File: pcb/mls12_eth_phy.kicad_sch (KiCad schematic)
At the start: 21 parts, among them U1 KSZ8081RNA, Y1 25MHz

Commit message: Update to 25W PoE+ module, 2 outputs
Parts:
- renumbered C13 to C11, C14 to C12, C15 to C13, C16 to C14, C17 to C15, C18 to C16, C19 to C17, C20 to C18, D5 to D6, FB13 to FB7, U1 to U2
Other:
- company: (none) -> Quomodo BV
- title: Ethernet & PoE -> Ethernet PHY
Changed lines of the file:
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@@
 	(paper "A4")
 	(title_block
-		(title "Ethernet & PoE")
-		(date "2025-07-25")
+		(title "Ethernet PHY")
+		(date "2025-07-26")
 		(rev "A")
+		(company "Quomodo BV")
 	)
 	(text "Ethernet routing checklist"
@@
 		(dnp no)
 		(fields_autoplaced yes)
-		(property "Reference" "#PWR017"
+		(property "Reference" "#PWR019"
 			(at 144.78 59.69 0)
 			(effects
@@
 			(project "mls12"
 				(path "/53bda2f8-fdf0-44f4-aced-3b46017d299c/f9d4ebc4-b22e-4ea3-9755-37111373d6cf"
-					(reference "#PWR017")
+					(reference "#PWR019")
 					(unit 1)
 				)
@@
 		(on_board yes)
 		(dnp no)
-		(property "Reference" "FB13"
+		(property "Reference" "FB7"
 			(at 132.08 39.624 90)
 			(effects
@@
 			(project "mls12"
 				(path "/53bda2f8-fdf0-44f4-aced-3b46017d299c/f9d4ebc4-b22e-4ea3-9755-37111373d6cf"
-					(reference "FB13")
+					(reference "FB7")
 					(unit 1)
 				)
@@
 		(dnp no)
 		(fields_autoplaced yes)
-		(property "Reference" "#PWR014"
+		(property "Reference" "#PWR016"
 			(at 127 41.91 0)
 			(effects
@@
 			(project "mls12"
 				(path "/53bda2f8-fdf0-44f4-aced-3b46017d299c/f9d4ebc4-b22e-4ea3-9755-37111373d6cf"
-					(reference "#PWR014")
+					(reference "#PWR016")
 					(unit 1)
 				)
@@
 		(dnp no)
 		(fields_autoplaced yes)
-		(property "Reference" "#PWR020"
+		(property "Reference" "#PWR022"
 			(at 157.48 77.47 0)
 			(effects
@@
 			(project "mls12"
 				(path "/53bda2f8-fdf0-44f4-aced-3b46017d299c/f9d4ebc4-b22e-4ea3-9755-37111373d6cf"
-					(reference "#PWR020")
+					(reference "#PWR022")
 					(unit 1)
 				)
@@
 		(dnp yes)
 		(fields_autoplaced yes)
-		(property "Reference" "C20"
+		(property "Reference" "C18"
 			(at 173.99 140.9699 0)
 			(effects
@@
 			(project "mls12"
 				(path "/53bda2f8-fdf0-44f4-aced-3b46017d299c/f9d4ebc4-b22e-4ea3-9755-37111373d6cf"
-					(reference "C20")
+					(reference "C18")
 					(unit 1)
 				)
@@
 		(dnp no)
 		(fields_autoplaced yes)
-		(property "Reference" "#PWR013"
+		(property "Reference" "#PWR015"
 			(at 114.3 138.43 0)
 			(effects
@@
 			(project "mls12"
 				(path "/53bda2f8-fdf0-44f4-aced-3b46017d299c/f9d4ebc4-b22e-4ea3-9755-37111373d6cf"
-					(reference "#PWR013")
+					(reference "#PWR015")
 					(unit 1)
 				)
@@
 		(dnp no)
 		(fields_autoplaced yes)
-		(property "Reference" "#PWR023"
+		(property "Reference" "#PWR025"
 			(at 213.36 107.95 0)
 			(effects
@@
 			(project "mls12"
 				(path "/53bda2f8-fdf0-44f4-aced-3b46017d299c/f9d4ebc4-b22e-4ea3-9755-37111373d6cf"
-					(reference "#PWR023")
+					(reference "#PWR025")
 					(unit 1)
 				)
@@
 		(dnp no)
 		(fields_autoplaced yes)
-		(property "Reference" "#PWR016"
+		(property "Reference" "#PWR018"
 			(at 135.89 138.43 0)
 			(effects
@@
 			(project "mls12"
 				(path "/53bda2f8-fdf0-44f4-aced-3b46017d299c/f9d4ebc4-b22e-4ea3-9755-37111373d6cf"
-					(reference "#PWR016")
+					(reference "#PWR018")
 					(unit 1)
 				)
@@
 		(dnp no)
 		(fields_autoplaced yes)
-		(property "Reference" "#PWR018"
+		(property "Reference" "#PWR020"
 			(at 144.78 77.47 0)
 			(effects
@@
 			(project "mls12"
 				(path "/53bda2f8-fdf0-44f4-aced-3b46017d299c/f9d4ebc4-b22e-4ea3-9755-37111373d6cf"
-					(reference "#PWR018")
+					(reference "#PWR020")
 					(unit 1)
 				)
@@
 		(dnp no)
 		(fields_autoplaced yes)
-		(property "Reference" "C18"
+		(property "Reference" "C16"
 			(at 161.29 64.7699 0)
 			(effects
@@
 			(project "mls12"
 				(path "/53bda2f8-fdf0-44f4-aced-3b46017d299c/f9d4ebc4-b22e-4ea3-9755-37111373d6cf"
-					(reference "C18")
+					(reference "C16")
 					(unit 1)
 				)
@@
 		(on_board yes)
 		(dnp no)
-		(property "Reference" "U1"
+		(property "Reference" "U2"
 			(at 133.7467 129.54 0)
 			(effects
@@
 			(project "mls12"
 				(path "/53bda2f8-fdf0-44f4-aced-3b46017d299c/f9d4ebc4-b22e-4ea3-9755-37111373d6cf"
-					(reference "U1")
+					(reference "U2")
 					(unit 1)
 				)
@@
 		(on_board yes)
 		(dnp no)
-		(property "Reference" "C13"
+		(property "Reference" "C11"
 			(at 110.49 64.7699 0)
 			(effects
@@
 			(project "mls12"
 				(path "/53bda2f8-fdf0-44f4-aced-3b46017d299c/f9d4ebc4-b22e-4ea3-9755-37111373d6cf"
-					(reference "C13")
+					(reference "C11")
 					(unit 1)
 				)
@@
 		(on_board yes)
 		(dnp no)
-		(property "Reference" "D5"
+		(property "Reference" "D6"
 			(at 241.3 110.4899 90)
 			(effects
@@
 			(project ""
 				(path "/53bda2f8-fdf0-44f4-aced-3b46017d299c/f9d4ebc4-b22e-4ea3-9755-37111373d6cf"
-					(reference "D5")
+					(reference "D6")
 					(unit 1)
 				)
@@
 		(on_board yes)
 		(dnp no)
-		(property "Reference" "C15"
+		(property "Reference" "C13"
 			(at 148.082 46.99 0)
 			(effects
@@
 			(project "mls12"
 				(path "/53bda2f8-fdf0-44f4-aced-3b46017d299c/f9d4ebc4-b22e-4ea3-9755-37111373d6cf"
-					(reference "C15")
+					(reference "C13")
 					(unit 1)
 				)
@@
 		(dnp no)
 		(fields_autoplaced yes)
-		(property "Reference" "#PWR024"
+		(property "Reference" "#PWR026"
 			(at 236.22 109.22 0)
 			(effects
@@
 			(project "mls12"
 				(path "/53bda2f8-fdf0-44f4-aced-3b46017d299c/f9d4ebc4-b22e-4ea3-9755-37111373d6cf"
-					(reference "#PWR024")
+					(reference "#PWR026")
 					(unit 1)
 				)
@@
 		(dnp no)
 		(fields_autoplaced yes)
-		(property "Reference" "#PWR019"
+		(property "Reference" "#PWR021"
 			(at 157.48 59.69 0)
 			(effects
@@
 			(project "mls12"
 				(path "/53bda2f8-fdf0-44f4-aced-3b46017d299c/f9d4ebc4-b22e-4ea3-9755-37111373d6cf"
-					(reference "#PWR019")
+					(reference "#PWR021")
 					(unit 1)
 				)
@@
 		(dnp yes)
 		(fields_autoplaced yes)
-		(property "Reference" "C19"
+		(property "Reference" "C17"
 			(at 173.99 125.7299 0)
 			(effects
@@
 			(project "mls12"
 				(path "/53bda2f8-fdf0-44f4-aced-3b46017d299c/f9d4ebc4-b22e-4ea3-9755-37111373d6cf"
-					(reference "C19")
+					(reference "C17")
 					(unit 1)
 				)
@@
 		(dnp no)
 		(fields_autoplaced yes)
-		(property "Reference" "C17"
+		(property "Reference" "C15"
 			(at 161.29 46.9899 0)
 			(effects
@@
 			(project "mls12"
 				(path "/53bda2f8-fdf0-44f4-aced-3b46017d299c/f9d4ebc4-b22e-4ea3-9755-37111373d6cf"
-					(reference "C17")
+					(reference "C15")
 					(unit 1)
 				)
@@
 		(dnp no)
 		(fields_autoplaced yes)
-		(property "Reference" "#PWR015"
+		(property "Reference" "#PWR017"
 			(at 127 77.47 0)
 			(effects
@@
 			(project "mls12"
 				(path "/53bda2f8-fdf0-44f4-aced-3b46017d299c/f9d4ebc4-b22e-4ea3-9755-37111373d6cf"
-					(reference "#PWR015")
+					(reference "#PWR017")
 					(unit 1)
 				)
@@
 		(dnp no)
 		(fields_autoplaced yes)
-		(property "Reference" "#PWR012"
+		(property "Reference" "#PWR014"
 			(at 114.3 77.47 0)
 			(effects
@@
 			(project "mls12"
 				(path "/53bda2f8-fdf0-44f4-aced-3b46017d299c/f9d4ebc4-b22e-4ea3-9755-37111373d6cf"
-					(reference "#PWR012")
+					(reference "#PWR014")
 					(unit 1)
 				)
@@
 		(on_board yes)
 		(dnp no)
-		(property "Reference" "C16"
+		(property "Reference" "C14"
 			(at 148.082 64.77 0)
 			(effects
@@
 			(project "mls12"
 				(path "/53bda2f8-fdf0-44f4-aced-3b46017d299c/f9d4ebc4-b22e-4ea3-9755-37111373d6cf"
-					(reference "C16")
+					(reference "C14")
 					(unit 1)
 				)
@@
 		(dnp no)
 		(fields_autoplaced yes)
-		(property "Reference" "#PWR021"
+		(property "Reference" "#PWR023"
 			(at 166.37 142.24 0)
 			(effects
@@
 			(project "mls12"
 				(path "/53bda2f8-fdf0-44f4-aced-3b46017d299c/f9d4ebc4-b22e-4ea3-9755-37111373d6cf"
-					(reference "#PWR021")
+					(reference "#PWR023")
 					(unit 1)
 				)
@@
 		(dnp no)
 		(fields_autoplaced yes)
-		(property "Reference" "#PWR022"
+		(property "Reference" "#PWR024"
 			(at 194.31 142.24 0)
 			(effects
@@
 			(project "mls12"
 				(path "/53bda2f8-fdf0-44f4-aced-3b46017d299c/f9d4ebc4-b22e-4ea3-9755-37111373d6cf"
-					(reference "#PWR022")
+					(reference "#PWR024")
 					(unit 1)
 				)
@@
 		(on_board yes)
 		(dnp no)
-		(property "Reference" "C14"
+		(property "Reference" "C12"
 			(at 123.698 64.77 0)
 			(effects
@@
 			(project "mls12"
 				(path "/53bda2f8-fdf0-44f4-aced-3b46017d299c/f9d4ebc4-b22e-4ea3-9755-37111373d6cf"
-					(reference "C14")
+					(reference "C12")
 					(unit 1)
 				)

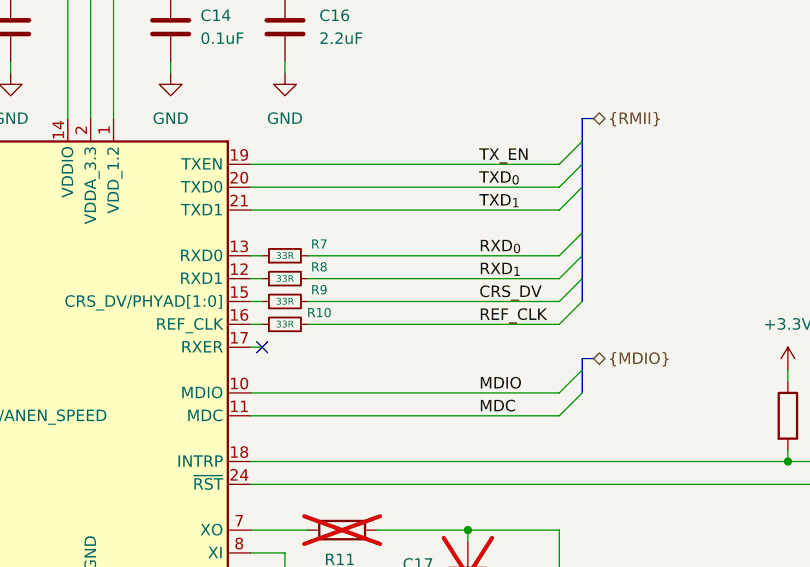
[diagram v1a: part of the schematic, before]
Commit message: Initial RMII, MDIO routing
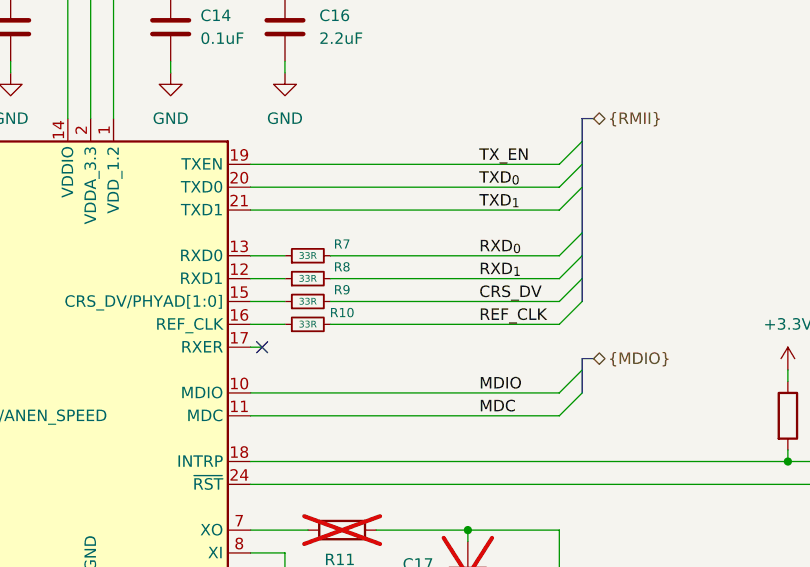
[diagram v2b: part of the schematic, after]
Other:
- moved on the sheet: R10, R7, R8, R9
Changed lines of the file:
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@@
 	(wire
 		(pts
-			(xy 160.02 99.06) (xy 187.96 99.06)
+			(xy 162.56 99.06) (xy 187.96 99.06)
 		)
 		(stroke
@@
 	(wire
 		(pts
-			(xy 160.02 91.44) (xy 187.96 91.44)
+			(xy 162.56 91.44) (xy 187.96 91.44)
 		)
 		(stroke
@@
 	(wire
 		(pts
-			(xy 153.67 93.98) (xy 154.94 93.98)
+			(xy 153.67 93.98) (xy 157.48 93.98)
 		)
 		(stroke
@@
 	(wire
 		(pts
-			(xy 153.67 99.06) (xy 154.94 99.06)
+			(xy 153.67 99.06) (xy 157.48 99.06)
 		)
 		(stroke
@@
 	(wire
 		(pts
-			(xy 160.02 96.52) (xy 187.96 96.52)
+			(xy 162.56 96.52) (xy 187.96 96.52)
 		)
 		(stroke
@@
 	(wire
 		(pts
-			(xy 160.02 93.98) (xy 187.96 93.98)
+			(xy 162.56 93.98) (xy 187.96 93.98)
 		)
 		(stroke
@@
 	(wire
 		(pts
-			(xy 153.67 96.52) (xy 154.94 96.52)
+			(xy 153.67 96.52) (xy 157.48 96.52)
 		)
 		(stroke
@@
 	(wire
 		(pts
-			(xy 153.67 91.44) (xy 154.94 91.44)
+			(xy 153.67 91.44) (xy 157.48 91.44)
 		)
 		(stroke
@@
 		(polyline
 			(pts
-				(xy 167.64 100.33) (xy 170.18 100.33) (xy 170.18 80.01) (xy 167.64 80.01)
+				(xy 156.21 100.33) (xy 175.26 100.33) (xy 175.26 80.01) (xy 156.21 80.01)
 			)
 			(stroke
@@
 		(length 2.54)
 		(shape round)
-		(at 168.91 80.01 0)
+		(at 163.83 80.01 0)
 		(fields_autoplaced yes)
 		(effects
@@
 		)
 		(property "Netclass" "RMII_50R"
-			(at 169.6085 77.47 0)
+			(at 164.5285 77.47 0)
 			(effects
 				(font
@@
 		)
 		(property "Component Class" ""
-			(at 408.94 8.89 0)
+			(at 403.86 8.89 0)
 			(effects
 				(font
@@
 	(symbol
 		(lib_id "Device:R_Small")
-		(at 157.48 93.98 90)
+		(at 160.02 93.98 90)
 		(unit 1)
 		(exclude_from_sim no)
@@
 		(dnp no)
 		(property "Reference" "R8"
-			(at 161.29 92.71 90)
+			(at 163.83 92.71 90)
 			(effects
 				(font
@@
 		)
 		(property "Value" "33R"
-			(at 157.48 93.98 90)
+			(at 160.02 93.98 90)
 			(effects
 				(font
@@
 		)
 		(property "Footprint" "Resistor_SMD:R_0603_1608Metric"
-			(at 157.48 93.98 0)
+			(at 160.02 93.98 0)
 			(effects
 				(font
@@
 		)
 		(property "Datasheet" "https://www.mouser.be/datasheet/2/210/ASC_WR-3314721.pdf"
-			(at 157.48 93.98 0)
+			(at 160.02 93.98 0)
 			(effects
 				(font
@@
 		)
 		(property "Description" "Resistor, small symbol"
-			(at 157.48 93.98 0)
+			(at 160.02 93.98 0)
 			(effects
 				(font
@@
 		)
 		(property "MF" "Walsin"
-			(at 157.48 93.98 90)
+			(at 160.02 93.98 90)
 			(effects
 				(font
@@
 		)
 		(property "MPN" "WR06X330 JTL"
-			(at 157.48 93.98 90)
+			(at 160.02 93.98 90)
 			(effects
 				(font
@@
 		)
 		(property "TODO" ""
-			(at 157.48 93.98 90)
+			(at 160.02 93.98 90)
 			(effects
 				(font
@@
 	(symbol
 		(lib_id "Device:R_Small")
-		(at 157.48 99.06 90)
+		(at 160.02 99.06 90)
 		(unit 1)
 		(exclude_from_sim no)
@@
 		(dnp no)
 		(property "Reference" "R10"
-			(at 161.29 97.79 90)
+			(at 163.83 97.79 90)
 			(effects
 				(font
@@
 		)
 		(property "Value" "33R"
-			(at 157.48 99.06 90)
+			(at 160.02 99.06 90)
 			(effects
 				(font
@@
 		)
 		(property "Footprint" "Resistor_SMD:R_0603_1608Metric"
-			(at 157.48 99.06 0)
+			(at 160.02 99.06 0)
 			(effects
 				(font
@@
 		)
 		(property "Datasheet" "https://www.mouser.be/datasheet/2/210/ASC_WR-3314721.pdf"
-			(at 157.48 99.06 0)
+			(at 160.02 99.06 0)
 			(effects
 				(font
@@
 		)
 		(property "Description" "Resistor, small symbol"
-			(at 157.48 99.06 0)
+			(at 160.02 99.06 0)
 			(effects
 				(font
@@
 		)
 		(property "MF" "Walsin"
-			(at 157.48 99.06 90)
+			(at 160.02 99.06 90)
 			(effects
 				(font
@@
 		)
 		(property "MPN" "WR06X330 JTL"
-			(at 157.48 99.06 90)
+			(at 160.02 99.06 90)
 			(effects
 				(font
@@
 		)
 		(property "TODO" ""
-			(at 157.48 99.06 90)
+			(at 160.02 99.06 90)
 			(effects
 				(font
@@
 	(symbol
 		(lib_id "Device:R_Small")
-		(at 157.48 96.52 90)
+		(at 160.02 96.52 90)
 		(unit 1)
 		(exclude_from_sim no)
@@
 		(dnp no)
 		(property "Reference" "R9"
-			(at 161.29 95.25 90)
+			(at 163.83 95.25 90)
 			(effects
 				(font
@@
 		)
 		(property "Value" "33R"
-			(at 157.48 96.52 90)
+			(at 160.02 96.52 90)
 			(effects
 				(font
@@
 		)
 		(property "Footprint" "Resistor_SMD:R_0603_1608Metric"
-			(at 157.48 96.52 0)
+			(at 160.02 96.52 0)
 			(effects
 				(font
@@
 		)
 		(property "Datasheet" "https://www.mouser.be/datasheet/2/210/ASC_WR-3314721.pdf"
-			(at 157.48 96.52 0)
+			(at 160.02 96.52 0)
 			(effects
 				(font
@@
 		)
 		(property "Description" "Resistor, small symbol"
-			(at 157.48 96.52 0)
+			(at 160.02 96.52 0)
 			(effects
 				(font
@@
 		)
 		(property "MF" "Walsin"
-			(at 157.48 96.52 90)
+			(at 160.02 96.52 90)
 			(effects
 				(font
@@
 		)
 		(property "MPN" "WR06X330 JTL"
-			(at 157.48 96.52 90)
+			(at 160.02 96.52 90)
 			(effects
 				(font
@@
 		)
 		(property "TODO" ""
-			(at 157.48 96.52 90)
+			(at 160.02 96.52 90)
 			(effects
 				(font
@@
 	(symbol
 		(lib_id "Device:R_Small")
-		(at 157.48 91.44 90)
+		(at 160.02 91.44 90)
 		(unit 1)
 		(exclude_from_sim no)
@@
 		(dnp no)
 		(property "Reference" "R7"
-			(at 161.29 90.17 90)
+			(at 163.83 90.17 90)
 			(effects
 				(font
@@
 		)
 		(property "Value" "33R"
-			(at 157.48 91.44 90)
+			(at 160.02 91.44 90)
 			(effects
 				(font
@@
 		)
 		(property "Footprint" "Resistor_SMD:R_0603_1608Metric"
-			(at 157.48 91.44 0)
+			(at 160.02 91.44 0)
 			(effects
 				(font
@@
 		)
 		(property "Datasheet" "https://www.mouser.be/datasheet/2/210/ASC_WR-3314721.pdf"
-			(at 157.48 91.44 0)
+			(at 160.02 91.44 0)
 			(effects
 				(font
@@
 		)
 		(property "Description" "Resistor, small symbol"
-			(at 157.48 91.44 0)
+			(at 160.02 91.44 0)
 			(effects
 				(font
@@
 		)
 		(property "MF" "Walsin"
-			(at 157.48 91.44 90)
+			(at 160.02 91.44 90)
 			(effects
 				(font
@@
 		)
 		(property "MPN" "WR06X330 JTL"
-			(at 157.48 91.44 90)
+			(at 160.02 91.44 90)
 			(effects
 				(font
@@
 		)
 		(property "TODO" ""
-			(at 157.48 91.44 90)
+			(at 160.02 91.44 90)
 			(effects
 				(font

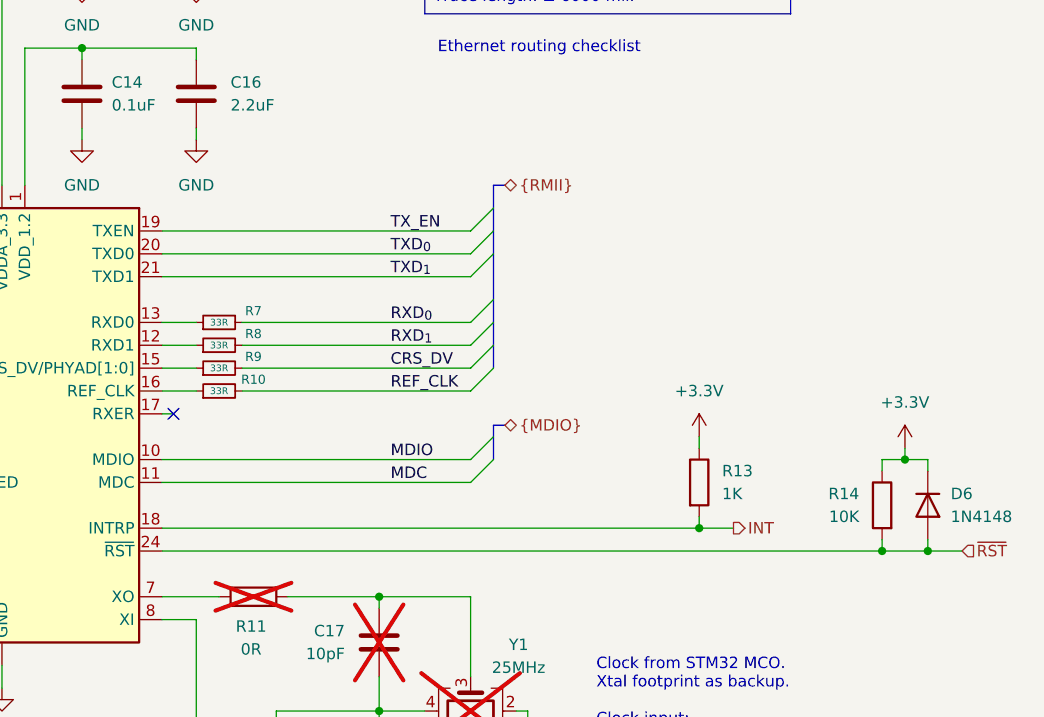
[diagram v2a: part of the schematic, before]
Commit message: Add test points
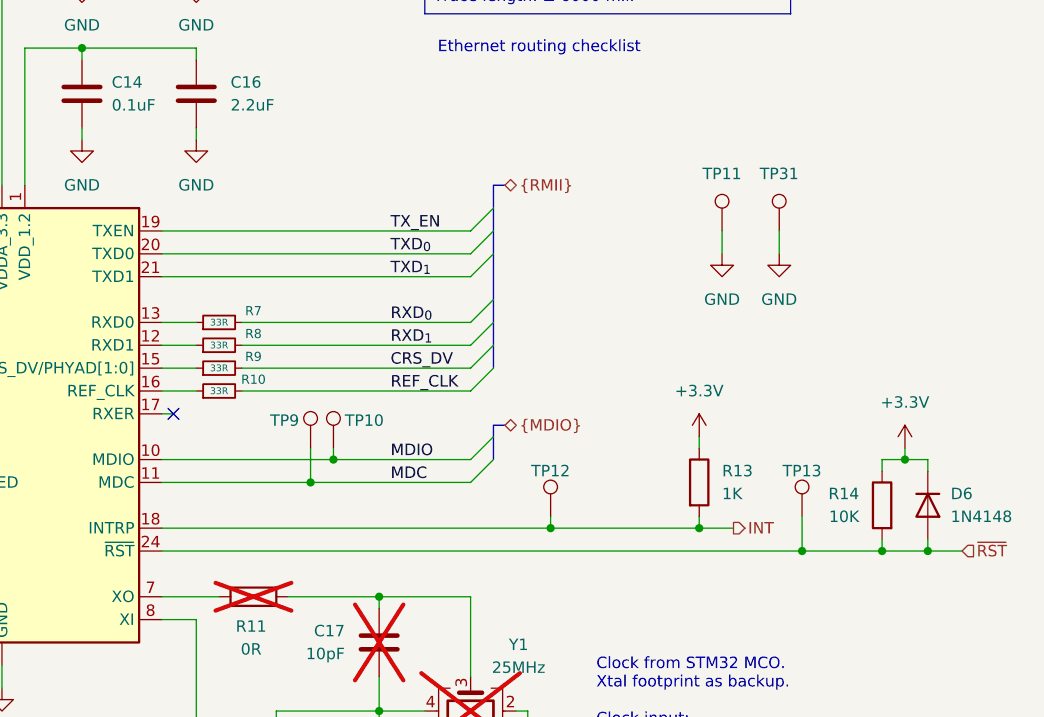
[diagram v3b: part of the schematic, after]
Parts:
- added TP10, TP12, TP13, TP9: TestPoint, TestPoint:TestPoint_Pad_D1.5mm, symbol Connector:TestPoint
- added TP11, TP31: TestPoint, TestPoint:TestPoint_Pad_1.5x1.5mm, symbol Connector:TestPoint
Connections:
- net GND: now also TP11.1, TP31.1
- net INT: now also TP12.1
- net MDC: now also TP9.1
- net MDIO: now also TP10.1
- net ~{RST}: now also TP13.1
